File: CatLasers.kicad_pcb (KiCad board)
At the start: 2 copper layers, 111.8 x 61 mm, 43 parts, among them J1 Piezzo, J2 Programmer, J3 Conn_01x04, J4 Conn_01x04, J5 Conn_01x20, J6 IR Emitter, J7 Power Jumper, J8 IR Receiver, J9 Conn_01x04, U1 MIC2288YD5-TR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

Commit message: DRC Pass
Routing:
- net 18V: track 202.7 -> 205.4 mm, vias 9 -> 7
- net GND: vias 12 -> 16
- net 3.3V: vias 2 -> 0
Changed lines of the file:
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@@
         (effects (font (size 1 1) (thickness 0.15)))
     )
-    (fp_text user "*" (at -5.6388 -2.9718 unlocked) (layer "F.SilkS")
-        (effects (font (size 1 1) (thickness 0.15)))
-    )
-    (fp_text user "*" (at -5.6388 -2.9718) (layer "F.SilkS")
+    (fp_text user "*" (at -5.08 -2.54) (layer "F.SilkS")
         (effects (font (size 1 1) (thickness 0.15)))
     )
@@
     (pad "39_9" smd rect (at -0.1 3.86) (size 0.9 0.9) (layers "F.Cu" "F.Paste" "F.Mask")
       (net 1 "GND") (pinfunction "GND") (pintype "power_in") (solder_mask_margin 0.102))
-    (pad "39_10" thru_hole circle (at -2.2 1.06) (size 0.3 0.3) (drill 0.2) (layers "*.Cu")
-      (net 1 "GND") (pinfunction "GND") (pintype "power_in"))
-    (pad "39_11" thru_hole circle (at -0.8 1.06) (size 0.3 0.3) (drill 0.2) (layers "*.Cu")
-      (net 1 "GND") (pinfunction "GND") (pintype "power_in"))
-    (pad "39_12" thru_hole circle (at -2.9 1.76) (size 0.3 0.3) (drill 0.2) (layers "*.Cu")
-      (net 1 "GND") (pinfunction "GND") (pintype "power_in"))
-    (pad "39_13" thru_hole circle (at -1.5 1.76) (size 0.3 0.3) (drill 0.2) (layers "*.Cu")
-      (net 1 "GND") (pinfunction "GND") (pintype "power_in"))
-    (pad "39_14" thru_hole circle (at -0.1 1.76) (size 0.3 0.3) (drill 0.2) (layers "*.Cu")
-      (net 1 "GND") (pinfunction "GND") (pintype "power_in"))
-    (pad "39_15" thru_hole circle (at -2.2 2.46) (size 0.3 0.3) (drill 0.2) (layers "*.Cu")
-      (net 1 "GND") (pinfunction "GND") (pintype "power_in"))
-    (pad "39_16" thru_hole circle (at -0.8 2.46) (size 0.3 0.3) (drill 0.2) (layers "*.Cu")
-      (net 1 "GND") (pinfunction "GND") (pintype "power_in"))
-    (pad "39_17" thru_hole circle (at -2.9 3.16) (size 0.3 0.3) (drill 0.2) (layers "*.Cu")
-      (net 1 "GND") (pinfunction "GND") (pintype "power_in"))
-    (pad "39_18" thru_hole circle (at -1.5 3.16) (size 0.3 0.3) (drill 0.2) (layers "*.Cu")
-      (net 1 "GND") (pinfunction "GND") (pintype "power_in"))
-    (pad "39_19" thru_hole circle (at -0.1 3.16) (size 0.3 0.3) (drill 0.2) (layers "*.Cu")
-      (net 1 "GND") (pinfunction "GND") (pintype "power_in"))
-    (pad "39_20" thru_hole circle (at -2.2 3.86) (size 0.3 0.3) (drill 0.2) (layers "*.Cu")
-      (net 1 "GND") (pinfunction "GND") (pintype "power_in"))
-    (pad "39_21" thru_hole circle (at -0.8 3.86) (size 0.3 0.3) (drill 0.2) (layers "*.Cu")
-      (net 1 "GND") (pinfunction "GND") (pintype "power_in"))
     (zone (net 0) (net_name "") (layer "F.Cu") (hatch full 0.508)
       (connect_pads (clearance 0))
@@
   (via (at 48.26 59.69) (size 0.8) (drill 0.4) (layers "F.Cu" "B.Cu") (net 1))
   (via (at 92.71 30.48) (size 0.8) (drill 0.4) (layers "F.Cu" "B.Cu") (net 1))
+  (via (at 82.55 39.37) (size 0.8) (drill 0.4) (layers "F.Cu" "B.Cu") (free) (net 1))
+  (via (at 85.09 39.37) (size 0.8) (drill 0.4) (layers "F.Cu" "B.Cu") (free) (net 1))
   (via (at 127 53.34) (size 0.8) (drill 0.4) (layers "F.Cu" "B.Cu") (net 1))
   (via (at 139.7 55.88) (size 0.8) (drill 0.4) (layers "F.Cu" "B.Cu") (net 1))
   (via (at 54.61 57.15) (size 0.8) (drill 0.4) (layers "F.Cu" "B.Cu") (net 1))
   (via (at 55.172268 52.645694) (size 0.8) (drill 0.4) (layers "F.Cu" "B.Cu") (net 1))
+  (via (at 85.09 34.29) (size 0.8) (drill 0.4) (layers "F.Cu" "B.Cu") (free) (net 1))
   (via (at 129.54 69.85) (size 0.8) (drill 0.4) (layers "F.Cu" "B.Cu") (net 1))
+  (via (at 82.55 34.29) (size 0.8) (drill 0.4) (layers "F.Cu" "B.Cu") (free) (net 1))
   (via (at 51.856 36.2375) (size 0.8) (drill 0.4) (layers "F.Cu" "B.Cu") (net 1))
   (via (at 78.74 48.26) (size 0.8) (drill 0.4) (layers "F.Cu" "B.Cu") (net 1))
   (via (at 62.23 29.21) (size 0.8) (drill 0.4) (layers "F.Cu" "B.Cu") (net 1))
   (via (at 74.93 29.21) (size 0.8) (drill 0.4) (layers "F.Cu" "B.Cu") (net 1))
+  (segment (start 57.15 31.75) (end 60.0685 31.75) (width 0.5) (layer "F.Cu") (net 2))
   (segment (start 101.6 74.93) (end 142.24 74.93) (width 0.5) (layer "F.Cu") (net 2))
+  (segment (start 60.0685 31.75) (end 60.3885 31.43) (width 0.5) (layer "F.Cu") (net 2))
   (segment (start 142.24 39.37) (end 142.24 39.5973) (width 0.5) (layer "F.Cu") (net 2))
   (segment (start 50.8 66.04) (end 101.6 66.04) (width 0.5) (layer "F.Cu") (net 2))
   (segment (start 36.83 40.65) (end 47 30.48) (width 0.5) (layer "F.Cu") (net 2))
+  (segment (start 55.499 30.48) (end 55.88 30.48) (width 0.5) (layer "F.Cu") (net 2))
   (segment (start 47 30.48) (end 50.8 30.48) (width 0.5) (layer "F.Cu") (net 2))
   (segment (start 140.97 51.1048) (end 140.0048 52.07) (width 0.5) (layer "F.Cu") (net 2))
+  (segment (start 55.88 30.48) (end 57.15 31.75) (width 0.5) (layer "F.Cu") (net 2))
   (segment (start 50.8 30.48) (end 50.8 31.75) (width 0.5) (layer "F.Cu") (net 2))
   (segment (start 50.8 30.48) (end 55.499 30.48) (width 0.5) (layer "F.Cu") (net 2))
-  (segment (start 56.769 31.75) (end 57.8485 31.75) (width 0.25) (layer "F.Cu") (net 2))
-  (segment (start 55.499 30.48) (end 56.769 31.75) (width 0.25) (layer "F.Cu") (net 2))
   (segment (start 140.97 50.8) (end 140.97 51.1048) (width 0.5) (layer "F.Cu") (net 2))
   (segment (start 142.24 39.5973) (end 140.9573 40.88) (width 0.5) (layer "F.Cu") (net 2))
   (via (at 50.8 66.04) (size 0.8) (drill 0.4) (layers "F.Cu" "B.Cu") (net 2))
   (via (at 50.8 31.75) (size 0.8) (drill 0.4) (layers "F.Cu" "B.Cu") (net 2))
-  (via (at 61.6585 33.02) (size 0.8) (drill 0.4) (layers "F.Cu" "B.Cu") (free) (net 2))
   (via (at 142.24 39.37) (size 0.8) (drill 0.4) (layers "F.Cu" "B.Cu") (net 2))
   (via (at 142.24 74.93) (size 0.8) (drill 0.4) (layers "F.Cu" "B.Cu") (net 2))
@@
   (via (at 101.6 74.93) (size 0.8) (drill 0.4) (layers "F.Cu" "B.Cu") (net 2))
   (via (at 101.6 66.04) (size 0.8) (drill 0.4) (layers "F.Cu" "B.Cu") (net 2))
-  (via (at 57.8485 31.75) (size 0.8) (drill 0.4) (layers "F.Cu" "B.Cu") (free) (net 2))
   (segment (start 142.24 52.07) (end 140.97 50.8) (width 0.5) (layer "B.Cu") (net 2))
   (segment (start 101.6 66.04) (end 101.6 74.93) (width 0.5) (layer "B.Cu") (net 2))
@@
   (segment (start 142.24 52.07) (end 142.24 39.37) (width 0.5) (layer "B.Cu") (net 2))
   (segment (start 50.8 31.75) (end 50.8 66.04) (width 0.5) (layer "B.Cu") (net 2))
-  (via (at 44.45 55.88) (size 0.8) (drill 0.4) (layers "F.Cu" "B.Cu") (free) (net 3))
-  (via (at 48.26 57.15) (size 0.8) (drill 0.4) (layers "F.Cu" "B.Cu") (free) (net 3))
   (segment (start 132.635 36.83) (end 135.89 36.83) (width 0.25) (layer "F.Cu") (net 4))
   (segment (start 132.6007 43.18) (end 132.6007 37.9057) (width 0.25) (layer "F.Cu") (net 4))
@@
   )
   (zone (net 3) (net_name "3.3V") (layer "F.Cu") (hatch edge 0.5)
-    (priority 2)
-    (connect_pads (clearance 0.5))
-    (min_thickness 0.25) (filled_areas_thickness no)
-    (fill yes (thermal_gap 0.5) (thermal_bridge_width 0.5))
-    (polygon
-      (pts
-        (xy 49.53 57.15)
-        (xy 54.229 57.15)
-        (xy 54.229 60.96)
-        (xy 47.879 60.96)
-        (xy 47.879 58.42)
-        (xy 43.18 58.42)
-        (xy 43.18 53.34)
-        (xy 46.99 53.34)
-        (xy 49.53 53.34)
-      )
-    )
-  )
-  (zone (net 3) (net_name "3.3V") (layer "F.Cu") (hatch edge 0.5)
     (connect_pads (clearance 0.5))
     (min_thickness 0.25) (filled_areas_thickness no)
@@
         (xy 60.3885 36.83)
         (xy 59.1185 36.83)
-        (xy 56.5785 36.83)
-        (xy 59.1185 38.1)
+        (xy 57.311166 36.204599)
+        (xy 57.311166 37.474599)
         (xy 59.1185 38.1)
         (xy 59.1185 39.37)
@@
         (xy 45.564649 52.336489)
         (xy 47.067957 52.329683)
-        (xy 49.607957 52.329683)
-        (xy 46.99 49.53)
+        (xy 48.864817 52.817679)
+        (xy 48.864817 51.287996)
         (xy 46.99 50.8)
         (xy 46.99 49.53)
@@
     (connect_pads (clearance 0))
     (min_thickness 0.25) (filled_areas_thickness no)
-    (keepout (tracks not_allowed) (vias not_allowed) (pads not_allowed) (copperpour not_allowed) (footprints not_allowed))
+    (keepout (tracks not_allowed) (vias not_allowed) (pads not_allowed) (copperpour not_allowed) (footprints allowed))
     (fill (thermal_gap 0.5) (thermal_bridge_width 0.5))
     (polygon

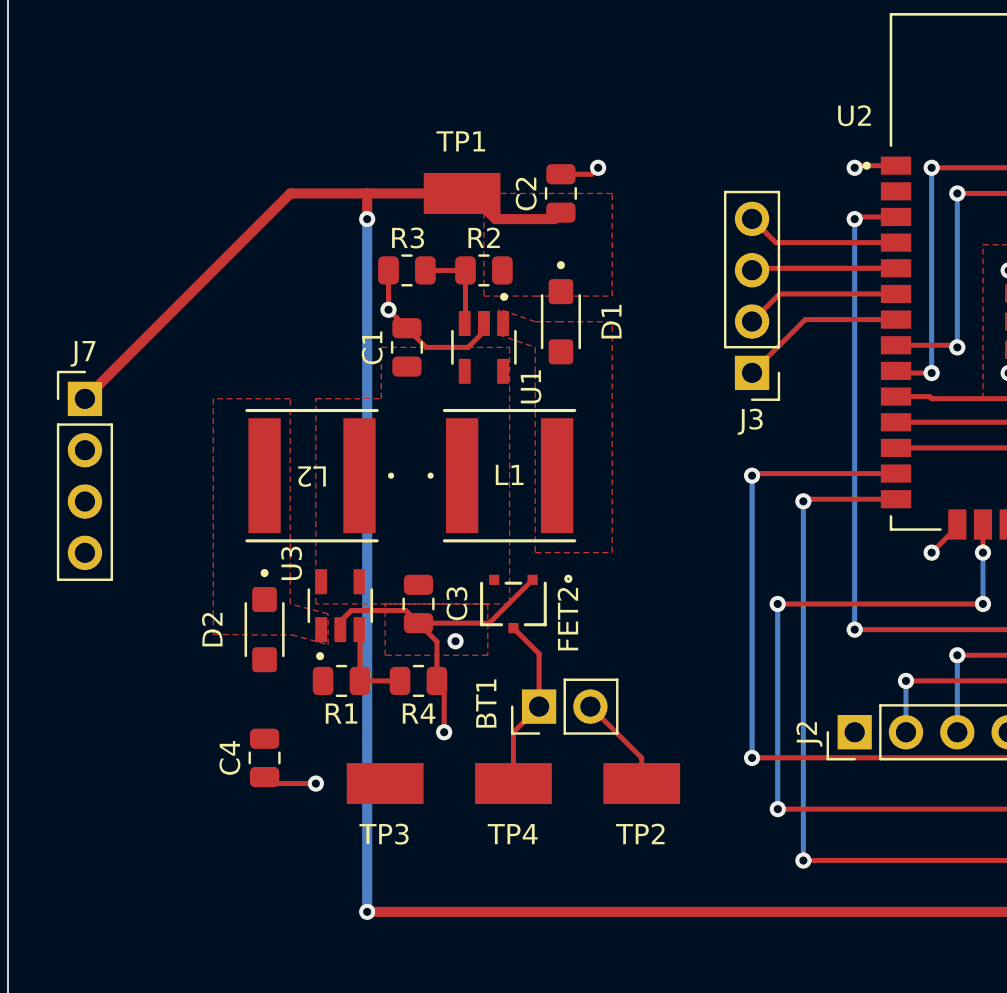
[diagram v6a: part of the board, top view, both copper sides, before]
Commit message: Extra Silk Screens
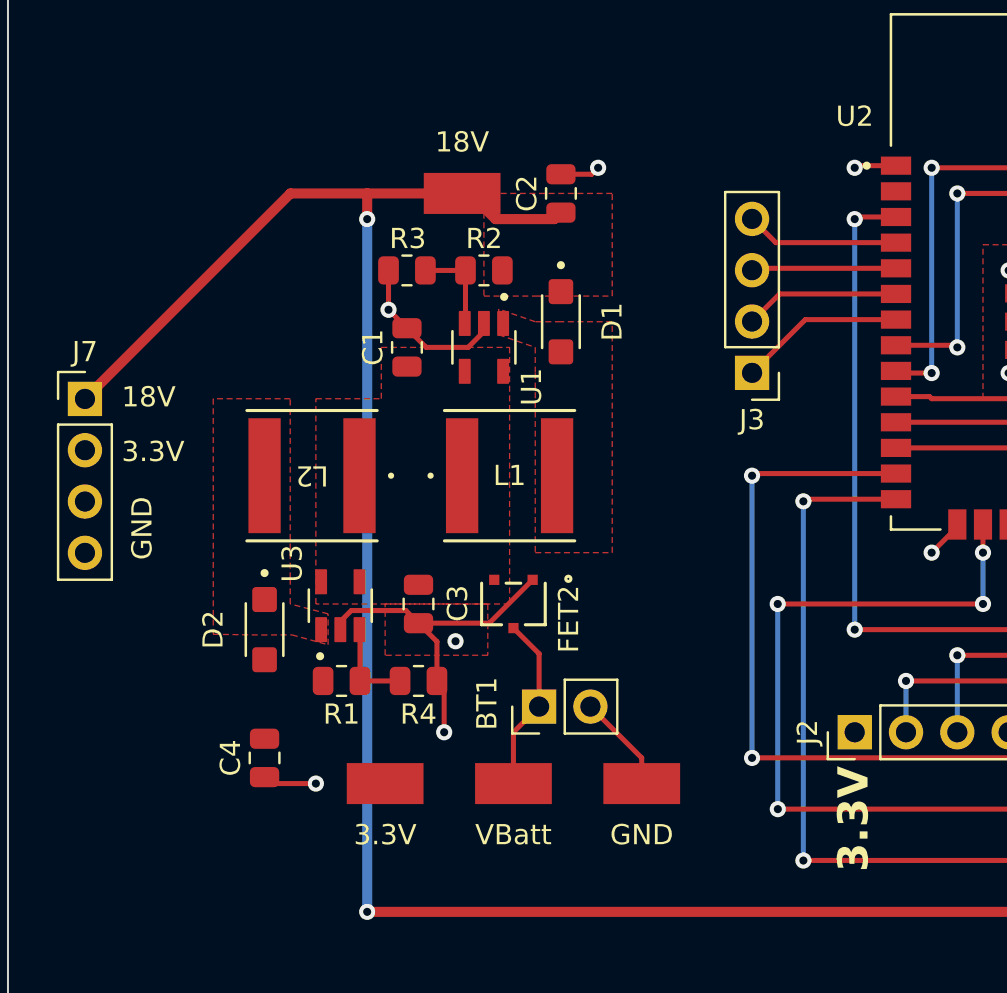
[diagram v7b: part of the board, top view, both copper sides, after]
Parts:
- renumbered TP1 to 18V, TP3 to 3.3V, TP2 to GND, TP4 to VBatt
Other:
- board text added: "18V"
- board text added: "3.3V"
- board text added: "GND"
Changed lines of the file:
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@@
     (property "ki_keywords" "test point tp")
     (attr smd)
-    (fp_text reference "TP2" (at 0 2.54) (layer "F.SilkS")
+    (fp_text reference "GND" (at 0 2.54) (layer "F.SilkS")
         (effects (font (size 1 1) (thickness 0.15)))
     )
@@
     (property "ki_keywords" "test point tp")
     (attr smd)
-    (fp_text reference "TP4" (at 0 -2.54) (layer "F.SilkS")
+    (fp_text reference "VBatt" (at 0 -2.54) (layer "F.SilkS")
         (effects (font (size 1 1) (thickness 0.15)))
     )
@@
     (property "ki_keywords" "test point tp")
     (attr smd)
-    (fp_text reference "TP3" (at 0 -2.54) (layer "F.SilkS")
+    (fp_text reference "3.3V" (at 0 -2.54) (layer "F.SilkS")
         (effects (font (size 1 1) (thickness 0.15)))
     )
@@
     (property "ki_keywords" "test point tp")
     (attr smd)
-    (fp_text reference "TP1" (at 0 -2.54) (layer "F.SilkS")
+    (fp_text reference "18V" (at 0 -2.54) (layer "F.SilkS")
         (effects (font (size 1 1) (thickness 0.15)))
     )
@@
   (gr_line (start 144.78 20.32) (end 144.78 78.74)
     (stroke (width 0.1) (type default)) (layer "Edge.Cuts"))
+  (gr_text "3.3V\n" (at 38.640977 43.847697) (layer "F.SilkS")
+    (effects (font (size 1 1) (thickness 0.15)) (justify left bottom))
+  )
+  (gr_text "GND\n" (at 40.244826 48.626843 90) (layer "F.SilkS")
+    (effects (font (size 1 1) (thickness 0.15)) (justify left bottom))
+  )
   (gr_text "15" (at 113.03 36.83) (layer "F.SilkS")
     (effects (font (size 1.5 1.5) (thickness 0.3) bold) (justify left bottom))
@@
     (effects (font (size 1 1) (thickness 0.15)) (justify left bottom))
   )
+  (gr_text "18V" (at 38.640977 41.142215) (layer "F.SilkS")
+    (effects (font (size 1 1) (thickness 0.15)) (justify left bottom))
+  )
+  (gr_text "3.3V" (at 75.74927 64.057771 90) (layer "F.SilkS")
+    (effects (font (size 1.5 1.5) (thickness 0.3) bold) (justify left bottom))
+  )
   (gr_text "5\n" (at 113.03 62.23) (layer "F.SilkS")

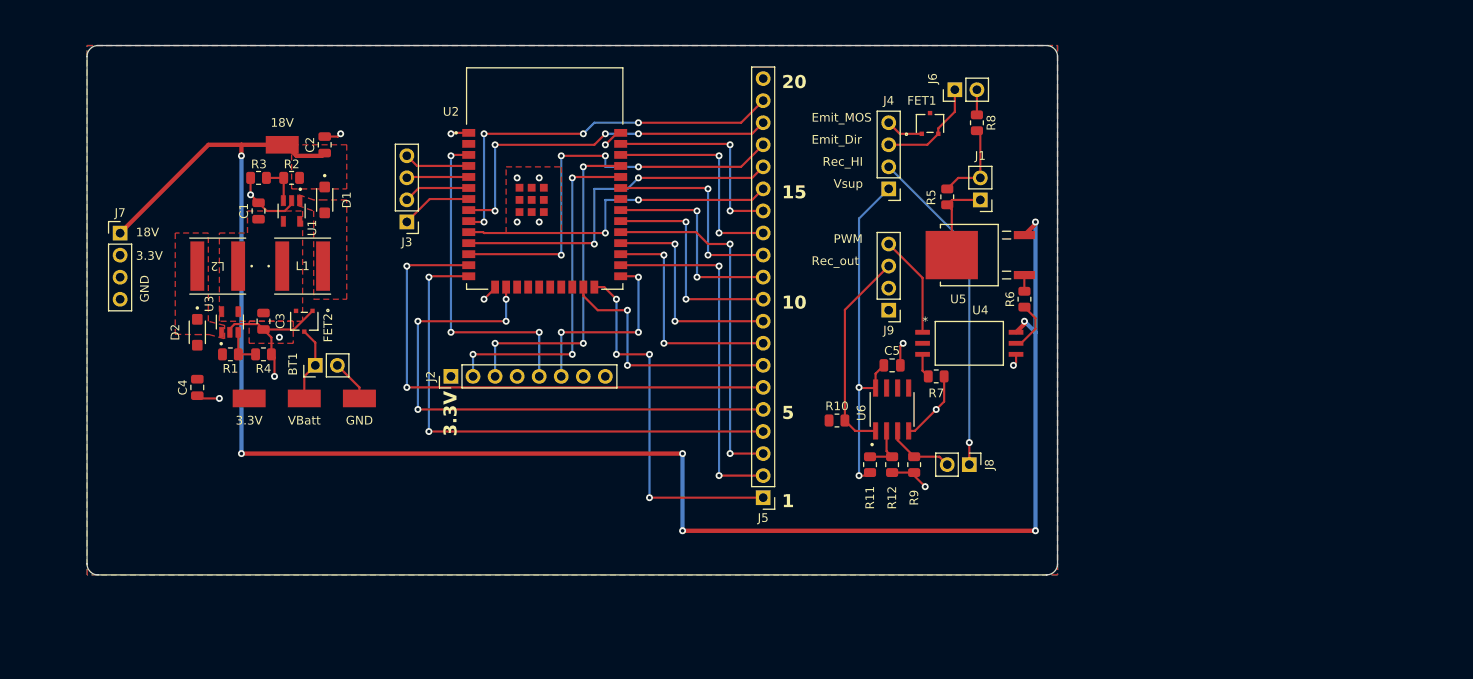
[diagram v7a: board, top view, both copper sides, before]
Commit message: Board Shortened
The price jumps significantly (some 400%) when the board crosses the threshold of 100mm in length
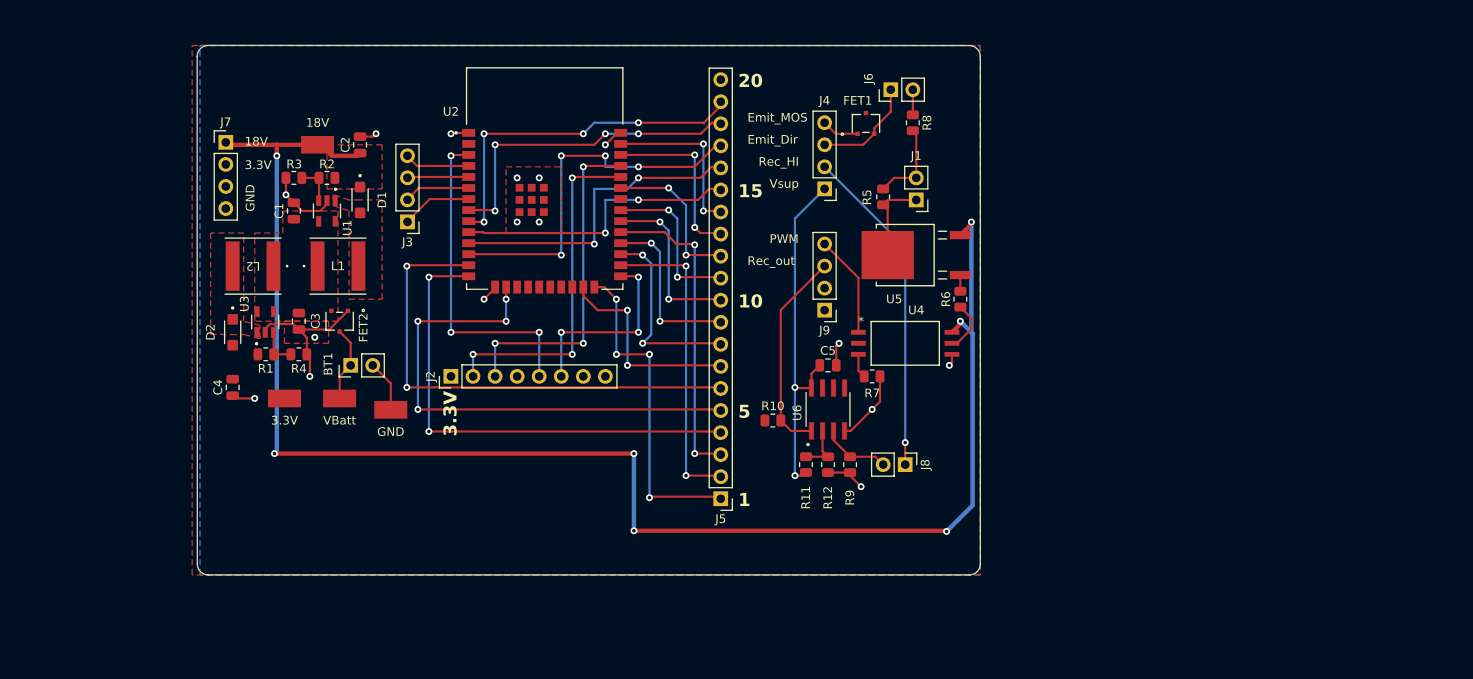
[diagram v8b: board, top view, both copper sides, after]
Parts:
- moved J7 16.0 mm to (49.0, 30.2)
- moved C5 7.38 mm to (118.3, 55.9)
- moved J4 7.38 mm to (118.0, 35.6)
- moved J6 7.38 mm to (125.6, 24.1)
- moved J8 7.38 mm to (127.2, 67.3)
- moved J9 7.38 mm to (118.0, 49.5)
- moved R12 7.38 mm to (118.3, 67.3)
- moved R5 7.38 mm to (124.7, 36.5)
- moved R9 7.38 mm to (120.9, 67.3)
- moved U4 7.38 mm to (127.2, 53.3)
- moved U5 7.38 mm to (127.2, 43.2)
- moved U6 7.38 mm to (118.3, 61.0)
- moved FET1 7.38 mm to (122.7, 28.0)
- moved J1 7.38 mm to (128.5, 36.8)
- moved R10 7.38 mm to (112.0, 62.2)
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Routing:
- net 18V: track 205.4 -> 180.5 mm
- net Net-(J5-Pin_12): track 24.1 -> 18.1 mm
- net Net-(J5-Pin_9): track 25.3 -> 19.9 mm
- net Net-(J5-Pin_11): track 24.1 -> 18.7 mm
- net Net-(J5-Pin_10): track 25.3 -> 20.0 mm
- net Net-(J5-Pin_13): track 25.3 -> 20.1 mm
- net Net-(J5-Pin_3): track 41.1 -> 36.2 mm
- net Net-(J5-Pin_16): track 41.4 -> 36.5 mm
- net Net-(J5-Pin_7): track 28.8 -> 23.9 mm
- net Net-(J5-Pin_6): track 62.2 -> 57.3 mm
- net Net-(J5-Pin_5): track 64.0 -> 59.1 mm
- net Net-(J5-Pin_4): track 60.9 -> 56.0 mm
- net Net-(J5-Pin_2): track 40.6 -> 35.7 mm
- net Net-(J5-Pin_18): track 42.6 -> 37.7 mm
- net Net-(J5-Pin_17): track 47.7 -> 42.8 mm
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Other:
- board size 111.8 x 61 mm -> 90.2 x 61 mm
